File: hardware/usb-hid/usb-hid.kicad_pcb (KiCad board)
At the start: 2 copper layers, 15 parts, among them J1 USB_A, J2 Conn_01x03_Female, J3 Conn_ARM_JTAG_SWD_10, U1 AMS1117-3.3, U2 NRF24L01_Breakout, U3 STM32F103C8Tx, Y1 Crystal

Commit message: Position the components
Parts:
- added C3: C, Capacitor_SMD:C_0603_1608Metric, B.Cu at (141.5, 107.0)
- added C4: C, Capacitor_SMD:C_0603_1608Metric, F.Cu at (132.5, 109.5)
- added C5: C, Capacitor_SMD:C_0603_1608Metric, F.Cu at (129.0, 109.5)
- added C6: C, Capacitor_SMD:C_0603_1608Metric, B.Cu at (138.0, 105.0)
- added J4: Ext_Power, Connector_PinHeader_2.00mm:PinHeader_1x03_P2.00mm_Vertical, F.Cu at (122.0, 104.5)
- added J5: GND, Connector_PinHeader_2.00mm:PinHeader_1x05_P2.00mm_Vertical, F.Cu at (130.5, 77.5)
- added J6: Extra_IO, Connector_PinHeader_2.00mm:PinHeader_1x05_P2.00mm_Vertical, F.Cu at (148.5, 108.5)
- added R4: 10k, Resistor_SMD:R_0603_1608Metric, B.Cu at (138.0, 108.5)
- added R5: 22, Resistor_SMD:R_0603_1608Metric, F.Cu at (128.0, 90.0)
- added R6: 22, Resistor_SMD:R_0603_1608Metric, F.Cu at (128.0, 88.0)
- added R7: 10k, Resistor_SMD:R_0603_1608Metric, F.Cu at (128.0, 84.5)
- added R8: 10k, Resistor_SMD:R_0603_1608Metric, B.Cu at (138.0, 102.5)
- added R9: 100k, Resistor_SMD:R_0603_1608Metric, B.Cu at (141.5, 105.0)
- added SW1: RESET_SW, Button_Switch_SMD:SW_SPST_TL3342, F.Cu at (141.0, 106.0)
- added SW2: EXT_SW, Button_Switch_SMD:SW_SPST_TL3342, F.Cu at (141.5, 98.0)
- C1, C2, R1, R2, U3, Y1: moved to B.Cu
- J1: value USB_A -> PC_USB
- J2: value Conn_01x03_Female -> Debug_UART; footprint Connector_PinHeader_2.00mm:PinHeader_1x03_P2.00mm_Horizontal -> Connector_PinHeader_2.00mm:PinHeader_1x03_P2.00mm_Vertical
- J3: value Conn_ARM_JTAG_SWD_10 -> MCU_SWD
- moved U2 101.5 mm to (148.5, 90.0), turned to 270 degrees
- moved C1 88.3 mm to (143.0, 102.5)
- moved U1 80.7 mm to (130.8, 104.1)
- moved Y1 73.2 mm to (143.0, 90.0), turned to 270 degrees
- moved U3 67.2 mm to (133.8, 89.3), turned to 90 degrees
- moved D1 64.8 mm to (134.5, 97.5), turned to 90 degrees
- moved R2 64.4 mm to (138.0, 97.5)
- moved R1 63.8 mm to (138.0, 100.0)
- moved D3 62.9 mm to (129.5, 97.5), turned to 90 degrees
- moved D2 61.0 mm to (132.0, 97.5), turned to 90 degrees
- moved C2 60.0 mm to (143.0, 77.5)
- moved J2 59.8 mm to (148.0, 77.5)
- moved J1 58.4 mm to (114.3, 88.9), turned to 180 degrees
- moved R3 56.8 mm to (126.2, 98.5), turned to 180 degrees
- moved J3 39.2 mm to (122.0, 77.5), turned to 90 degrees
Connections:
- D1 pad 1: GND -> Net-(D1-Pad1)
- D2 pad 1: GND -> Net-(D2-Pad1)
- D3 pad 1: GND -> Net-(D3-Pad1)
- J1 pad 2: /USB_D- -> Net-(J1-Pad2)
- J1 pad 3: /USB_D+ -> Net-(J1-Pad3)
- R1 pad 1: Net-(D1-Pad2) -> GND
- R1 pad 2: Net-(R1-Pad2) -> Net-(D1-Pad1)
- R2 pad 1: Net-(D2-Pad2) -> GND
- R2 pad 2: Net-(R2-Pad2) -> Net-(D2-Pad1)
- R3 pad 1: Net-(D3-Pad2) -> GND
- R3 pad 2: Net-(R3-Pad2) -> Net-(D3-Pad1)
- U3 pad 10: Net-(R1-Pad2) -> Net-(D1-Pad2)
- U3 pad 11: Net-(R2-Pad2) -> Net-(D2-Pad2)
- U3 pad 12: Net-(R3-Pad2) -> Net-(D3-Pad2)
- U3 pad 18: Net-(U3-Pad18) -> /PWM1
- U3 pad 19: Net-(U3-Pad19) -> /PWM2
- U3 pad 25: Net-(U3-Pad25) -> Net-(U2-Pad4)
- U3 pad 29: Net-(U3-Pad29) -> Net-(U2-Pad8)
- U3 pad 30: Net-(U3-Pad30) -> Net-(U2-Pad3)
- U3 pad 9: Net-(U3-Pad9) -> VCC

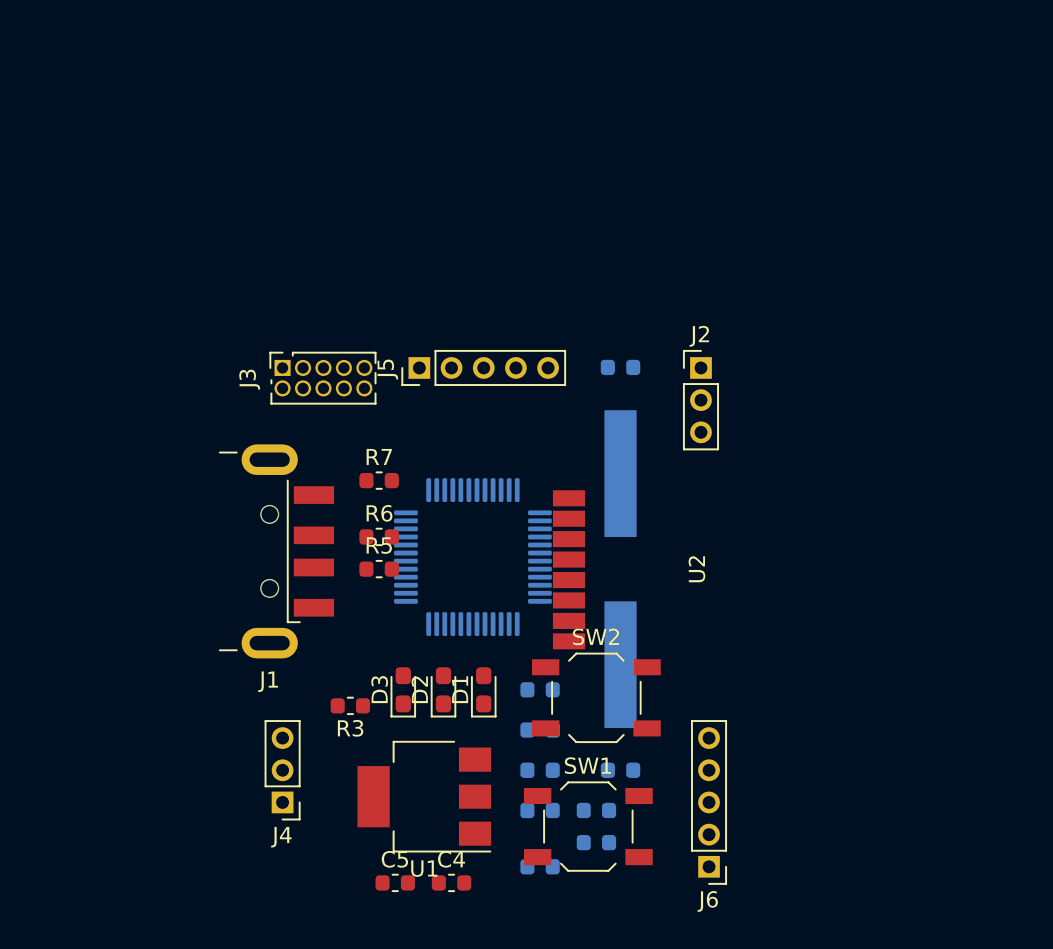
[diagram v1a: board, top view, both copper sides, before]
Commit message: Add new components and make the sizes proper
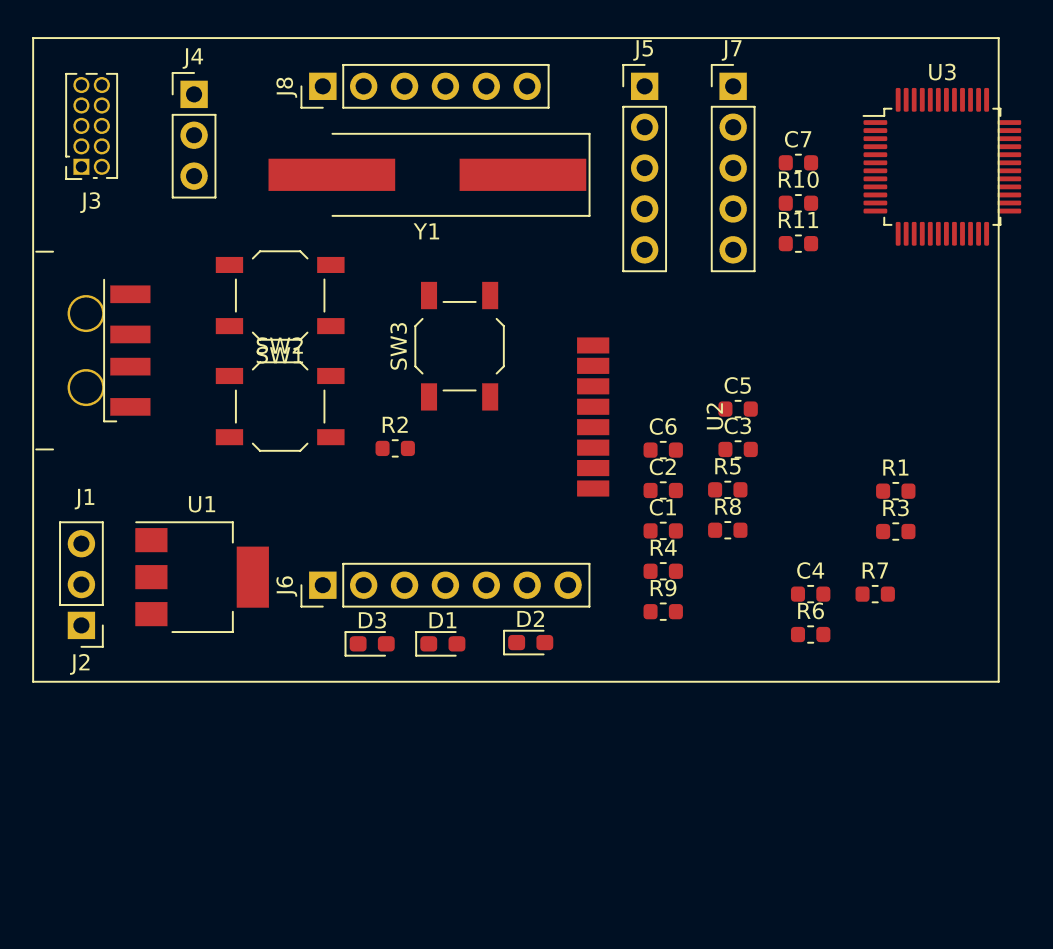
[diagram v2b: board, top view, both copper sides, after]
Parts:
- added C7: C, Capacitor_SMD:C_0603_1608Metric, F.Cu at (154.1, 64.8)
- added J7: Extra-IO-2, Connector_PinHeader_2.54mm:PinHeader_1x05_P2.54mm_Vertical, F.Cu at (150.0, 60.0)
- added J8: Extra-IO-0, Connector_PinHeader_2.54mm:PinHeader_1x06_P2.54mm_Vertical, F.Cu at (124.5, 60.0)
- added R10: 10k, Resistor_SMD:R_0603_1608Metric, F.Cu at (154.1, 67.3)
- added R11: 100k, Resistor_SMD:R_0603_1608Metric, F.Cu at (154.1, 69.8)
- added SW3: EXT_SW, Button_Switch_SMD:SW_SPST_TL3342, F.Cu at (133.0, 76.2)
- C1, C2, C3, C6, R1, R2, R4, R8, R9, U3, Y1: moved to F.Cu
- J1: footprint Connector_USB:USB_A_CNCTech_1001-011-01101_Horizontal -> Connector_USB:USB_A_2.3_2
- J2, J4: footprint Connector_PinHeader_2.00mm:PinHeader_1x03_P2.00mm_Vertical -> Connector_PinHeader_2.54mm:PinHeader_1x03_P2.54mm_Vertical
- J5: footprint Connector_PinHeader_2.00mm:PinHeader_1x05_P2.00mm_Vertical -> Connector_PinHeader_2.54mm:PinHeader_1x05_P2.54mm_Vertical
- J6: value Extra_IO -> Extra-IO-1; footprint Connector_PinHeader_2.00mm:PinHeader_1x05_P2.00mm_Vertical -> Connector_PinHeader_2.54mm:PinHeader_1x07_P2.54mm_Vertical
- moved J4 44.3 mm to (116.5, 60.5), turned to 0 degrees
- moved J2 41.7 mm to (109.5, 93.5), turned to 180 degrees
- moved SW1 38.2 mm to (121.8, 73.0), turned to 180 degrees
- moved U3 37.9 mm to (163.0, 65.0), turned to 0 degrees
- moved C5 36.3 mm to (150.3, 80.1)
- moved R3 35.6 mm to (160.1, 87.7), turned to 0 degrees
- moved R7 31.6 mm to (158.8, 91.6)
- moved J6 29.7 mm to (124.5, 91.0), turned to 90 degrees
- moved C4 28.6 mm to (154.8, 91.6)
- moved R6 27.5 mm to (154.8, 94.1)
- moved Y1 27.3 mm to (131.0, 65.5), turned to 180 degrees
- moved SW2 26.7 mm to (121.8, 79.9)
- moved R1 26.6 mm to (160.1, 85.2)
- moved C3 26.0 mm to (150.3, 82.6)
- moved C6 23.7 mm to (145.7, 82.6)
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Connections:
- J6 pad 1: /PWM1 -> Net-(J6-Pad1)
- J6 pad 2: /PWM2 -> Net-(J6-Pad2)
- U3 pad 15: Net-(J6-Pad3) -> Net-(J7-Pad2)
- U3 pad 16: Net-(J6-Pad4) -> Net-(J7-Pad3)
- U3 pad 17: Net-(J6-Pad5) -> Net-(J7-Pad4)
- U3 pad 18: /PWM1 -> Net-(J6-Pad4)
- U3 pad 19: /PWM2 -> Net-(J6-Pad3)
- U3 pad 2: Net-(U3-Pad2) -> Net-(J6-Pad7)
- U3 pad 20: Net-(U3-Pad20) -> Net-(J6-Pad2)
- U3 pad 3: Net-(U3-Pad3) -> Net-(J6-Pad6)
- U3 pad 39: Net-(U3-Pad39) -> Net-(J6-Pad1)
- U3 pad 4: Net-(U3-Pad4) -> Net-(J6-Pad5)

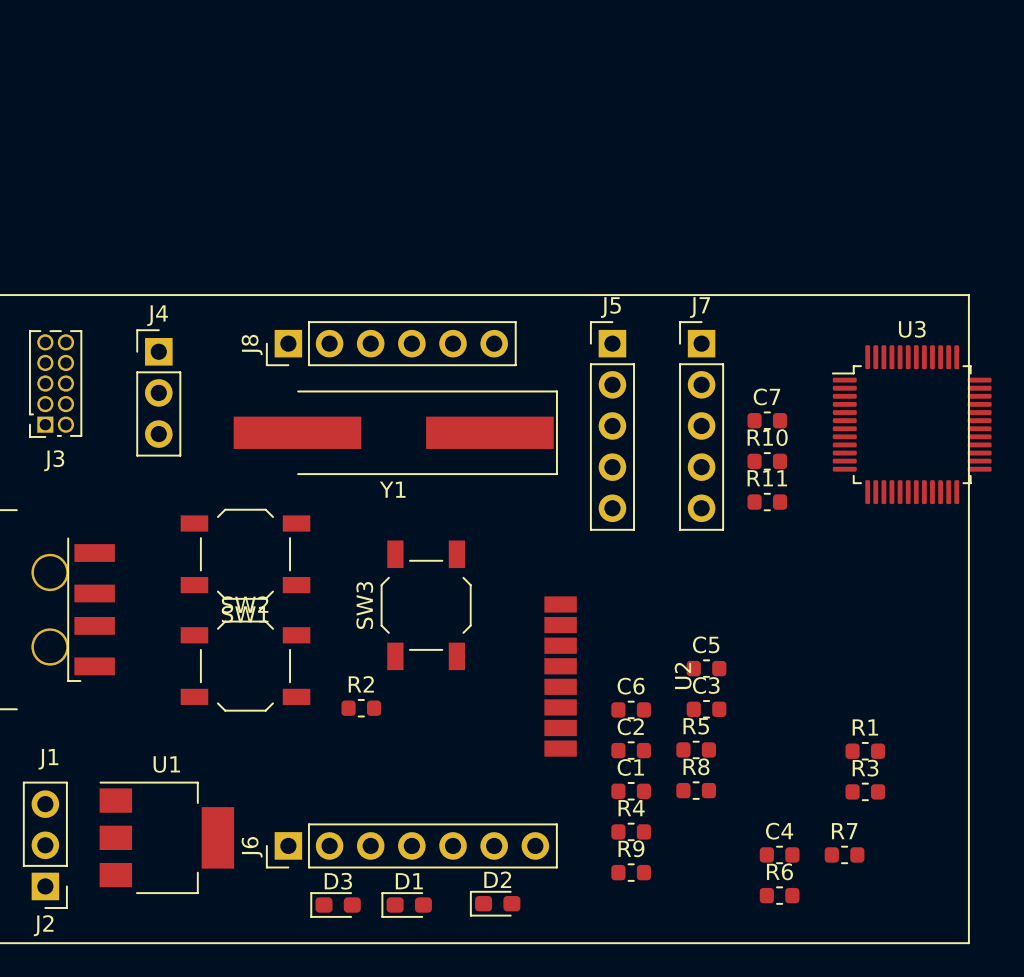
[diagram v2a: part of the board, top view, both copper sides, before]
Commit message: Restruct the schematic for better symbols
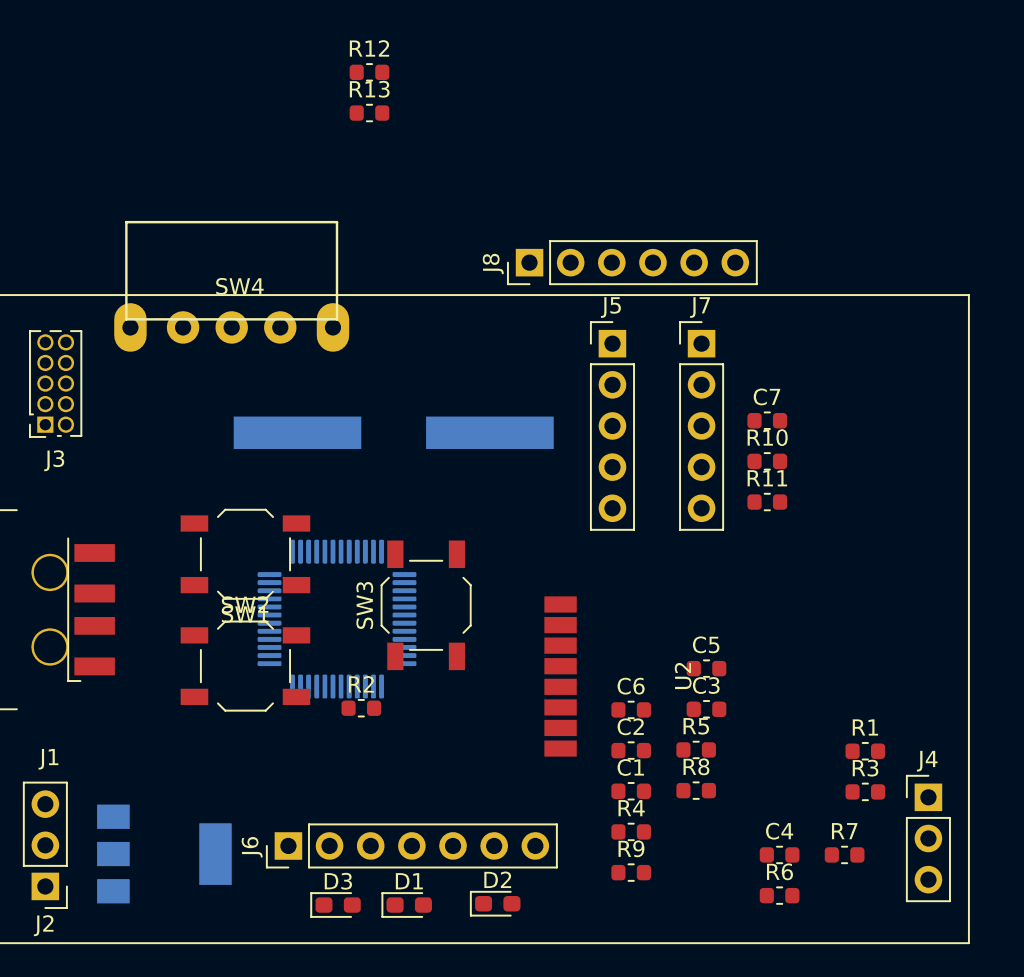
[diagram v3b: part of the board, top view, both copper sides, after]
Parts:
- added R12: 0, Resistor_SMD:R_0603_1608Metric, F.Cu at (129.5, 43.3)
- added R13: 0, Resistor_SMD:R_0603_1608Metric, F.Cu at (129.5, 45.8)
- added SW4: Power_SW, custom_lib:Switch-SS12F23, F.Cu at (121.0, 59.0)
- U1, U3, Y1: moved to B.Cu
- moved J4 54.9 mm to (164.0, 88.0)
- moved U3 37.5 mm to (127.5, 77.0), turned to 180 degrees
- moved J8 15.7 mm to (139.4, 55.0)
- moved U1 1.01 mm to (116.8, 91.5)
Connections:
- J4 pad 1: VCC -> Net-(J4-Pad1)
- J4 pad 3: Net-(J1-Pad1) -> Net-(J4-Pad3)

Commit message: Finish layout
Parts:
- removed R12, R13: 0, Resistor_SMD:R_0603_1608Metric
- added C8: C, Capacitor_SMD:C_0603_1608Metric, F.Cu at (60.1, 79.7)
- C1, C2, C3, C4, C5, R1, R2, R3: moved to B.Cu
- J5: value GND -> Extra-IO-2; footprint Connector_PinHeader_2.54mm:PinHeader_1x05_P2.54mm_Vertical -> Connector_PinHeader_2.54mm:PinHeader_1x06_P2.54mm_Vertical
- J6: footprint Connector_PinHeader_2.54mm:PinHeader_1x07_P2.54mm_Vertical -> Connector_PinHeader_2.54mm:PinHeader_1x06_P2.54mm_Vertical
- J7: value Extra-IO-2 -> Conn_01x02_Female; footprint Connector_PinHeader_2.54mm:PinHeader_1x05_P2.54mm_Vertical -> Connector_PinHeader_2.54mm:PinHeader_1x02_P2.54mm_Vertical
- R10: value 10k -> 22; moved to B.Cu
- R11: value 100k -> 22
- R4, R8: value 10k -> 22
- R7: value 10k -> 1.5k
- SW1: value RESET_SW -> E_SW
- SW2: value EXT_SW -> Reset
- SW3: value EXT_SW -> Boot
- SW4: footprint custom_lib:Switch-SS12F23 -> Button_Switch_THT:SW_Aliexpress_3pin
- U2: value NRF24L01_Breakout -> STM32F103C8; footprint mysensors_radios:NRF24L01-SMD -> mcu:QFP50P900X900X160-48N; moved to B.Cu
- U3: value STM32F103C8Tx -> NRF24L01_SMD; footprint Package_QFP:LQFP-48_7x7mm_P0.5mm -> mysensors_radios:NRF24L01_SMD_PinChange; moved to F.Cu
- moved R7 115.9 mm to (45.9, 65.5), turned to 180 degrees
- moved R1 114.3 mm to (47.3, 66.8)
- moved R6 112.1 mm to (45.9, 67.3), turned to 180 degrees
- moved C4 110.9 mm to (44.1, 85.6)
- moved J7 109.1 mm to (45.5, 91.3), turned to 270 degrees
- moved C7 108.2 mm to (45.9, 63.6), turned to 180 degrees
- moved C2 106.9 mm to (42.3, 57.9)
- moved C5 106.5 mm to (44.1, 87.8)
- moved R5 105.0 mm to (45.9, 69.1), turned to 180 degrees
- moved R9 104.4 mm to (45.9, 61.8), turned to 180 degrees
- moved R3 99.5 mm to (63.6, 63.4), turned to 180 degrees
- moved R11 98.0 mm to (56.1, 66.2)
- moved C6 97.3 mm to (49.7, 66.7)
- moved C3 96.6 mm to (53.9, 75.7)
- moved J4 95.5 mm to (68.6, 91.2), turned to 90 degrees
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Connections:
- C3 pad 1: Net-(C3-Pad1) -> VCC
- C3 pad 2: GND -> /SW_conn
- C6 pad 1: VCC -> /NRST
- C6 pad 2: Net-(C6-Pad2) -> GND
- C7 pad 1: VCC -> /Boot1
- C7 pad 2: Net-(C7-Pad2) -> GND
- D1 pad 1: Net-(D1-Pad1) -> GND
- D2 pad 1: Net-(D2-Pad1) -> GND
- D3 pad 1: Net-(D3-Pad1) -> GND
- J3 pad 10: Net-(J3-Pad10) -> (no net)
- J3 pad 2: Net-(J3-Pad2) -> /SWDIO_Conn
- J3 pad 4: Net-(J3-Pad4) -> /SWDCLK_Conn
- J3 pad 6: Net-(J3-Pad6) -> (no net)
- J3 pad 7: Net-(J3-Pad7) -> (no net)
- J3 pad 8: Net-(J3-Pad8) -> (no net)
- J3 pad 9: Net-(J3-Pad9) -> (no net)
- J5 pad 1: GND -> Net-(J5-Pad1)
- J5 pad 2: GND -> Net-(J5-Pad2)
- J5 pad 3: GND -> Net-(J5-Pad3)
- J5 pad 4: GND -> Net-(J5-Pad4)
- J5 pad 5: GND -> Net-(J5-Pad5)
- J7 pad 1: Net-(J7-Pad1) -> VCC
- J7 pad 2: Net-(J7-Pad2) -> GND
- R1 pad 1: GND -> Net-(D1-Pad2)
- R1 pad 2: Net-(D1-Pad1) -> Net-(R1-Pad2)
- R10 pad 1: Net-(C7-Pad2) -> GND
- R11 pad 1: GND -> /NRST
- R11 pad 2: Net-(R10-Pad2) -> VCC
- R2 pad 1: GND -> Net-(D2-Pad2)
- R2 pad 2: Net-(D2-Pad1) -> Net-(R2-Pad2)
- R3 pad 1: GND -> Net-(D3-Pad2)
- R3 pad 2: Net-(D3-Pad1) -> Net-(R3-Pad2)
- R4 pad 1: Net-(C3-Pad1) -> /SW_conn
- R4 pad 2: VCC -> Net-(R4-Pad2)
- R8 pad 1: Net-(C6-Pad2) -> GND
- R8 pad 2: Net-(R8-Pad2) -> Net-(R4-Pad2)
- R9 pad 1: GND -> /Boot1
- R9 pad 2: Net-(R8-Pad2) -> GND
- SW1 pad 1: GND -> VCC
- SW1 pad 2: Net-(C3-Pad1) -> Net-(R4-Pad2)
- SW2 pad 1: VCC -> /NRST
- SW2 pad 2: Net-(R8-Pad2) -> GND
- SW3 pad 2: Net-(R10-Pad2) -> /Boot1
- SW4 pad 2: Net-(R12-Pad1) -> Net-(J1-Pad1)
- U2 pad 1: GND -> VCC
- U2 pad 2: VCC -> Net-(J8-Pad6)
- U2 pad 3: Net-(U2-Pad3) -> Net-(J8-Pad5)
- U2 pad 4: Net-(U2-Pad4) -> Net-(J8-Pad4)
- U2 pad 5: Net-(U2-Pad5) -> Net-(C2-Pad2)
- U2 pad 6: Net-(U2-Pad6) -> Net-(C1-Pad2)
- U2 pad 7: Net-(U2-Pad7) -> /NRST
- U2 pad 8: Net-(U2-Pad8) -> GND
- U3 pad 1: Net-(U3-Pad1) -> VCC
- U3 pad 2: Net-(J6-Pad7) -> GND
- U3 pad 3: Net-(J6-Pad6) -> Net-(U2-Pad30)
- U3 pad 4: Net-(J6-Pad5) -> Net-(U2-Pad29)
- U3 pad 5: Net-(C2-Pad2) -> Net-(U2-Pad26)
- U3 pad 6: Net-(C1-Pad2) -> Net-(U2-Pad28)
- U3 pad 7: Net-(C3-Pad1) -> Net-(U2-Pad27)
- U3 pad 8: GND -> Net-(U2-Pad25)
- Y1 pad 1: Net-(C1-Pad2) -> Net-(C2-Pad2)
- Y1 pad 2: Net-(C2-Pad2) -> Net-(C1-Pad2)
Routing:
- net GND: track 0.00 -> 265.9 mm, vias 0 -> 4
- net VCC: track 0.00 -> 115.3 mm, vias 0 -> 5
- net Net-(U2-Pad25): track 0.00 -> 56.2 mm, vias 0 -> 1
- net Net-(U2-Pad27): track 0.00 -> 56.1 mm, vias 0 -> 1
- net Net-(J1-Pad1): track 0.00 -> 41.0 mm, vias 0 -> 1
- net /SWDCLK_Conn: track 0.00 -> 37.2 mm, vias 0 -> 1
- net Net-(J6-Pad6): track 0.00 -> 27.8 mm, vias 0 -> 1
- net /SWDIO_Conn: track 0.00 -> 26.4 mm, vias 0 -> 1
- net Net-(J6-Pad5): track 0.00 -> 26.2 mm, vias 0 -> 1
- net Net-(J6-Pad4): track 0.00 -> 23.7 mm, vias 0 -> 1
- net Net-(J6-Pad3): track 0.00 -> 22.4 mm, vias 0 -> 1
- net Net-(J5-Pad6): track 0.00 -> 21.4 mm
- net Net-(J6-Pad2): track 0.00 -> 20.6 mm, vias 0 -> 1
- net Net-(J5-Pad5): track 0.00 -> 19.6 mm
- net Net-(J6-Pad1): track 0.00 -> 19.3 mm, vias 0 -> 1
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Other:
- board outline added: 40.9 x 44.5 mm

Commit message: Move components
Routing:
- added copper zone on B.Cu, net GND
- added copper zone on F.Cu, net GND
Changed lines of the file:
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@@
   (page A4)
   (layers
-    (0 F.Cu signal)
+    (0 F.Cu signal hide)
     (31 B.Cu signal)
     (32 B.Adhes user hide)
-    (33 F.Adhes user hide)
-    (34 B.Paste user)
-    (35 F.Paste user hide)
+    (33 F.Adhes user)
+    (34 B.Paste user hide)
+    (35 F.Paste user)
     (36 B.SilkS user hide)
-    (37 F.SilkS user hide)
-    (38 B.Mask user)
-    (39 F.Mask user hide)
-    (40 Dwgs.User user)
+    (37 F.SilkS user)
+    (38 B.Mask user hide)
+    (39 F.Mask user)
+    (40 Dwgs.User user hide)
     (41 Cmts.User user)
     (42 Eco1.User user)
@@
     (44 Edge.Cuts user)
     (45 Margin user)
-    (46 B.CrtYd user)
+    (46 B.CrtYd user hide)
     (47 F.CrtYd user)
     (48 B.Fab user hide)
@@
   (segment (start 60.8 63.4) (end 62.8 63.4) (width 0.25) (layer B.Cu) (net 50))
   (segment (start 59.78 64.05) (end 60.15 64.05) (width 0.25) (layer B.Cu) (net 50))
+  (zone (net 1) (net_name GND) (layer B.Cu) (hatch edge 0.508)
+    (connect_pads (clearance 0.508))
+    (min_thickness 0.254)
+    (fill yes (arc_segments 32) (thermal_gap 0.508) (thermal_bridge_width 0.508))
+    (polygon
+      (pts
+        (xy 76.65 93.55) (xy 35.85 93.55) (xy 35.8 49.1) (xy 76.7 49.1)
+      )
+    )
+  )
+  (zone (net 1) (net_name GND) (layer F.Cu) (hatch edge 0.508)
+    (connect_pads (clearance 0.508))
+    (min_thickness 0.254)
+    (fill yes (arc_segments 32) (thermal_gap 0.508) (thermal_bridge_width 0.508))
+    (polygon
+      (pts
+        (xy 76.7 49.15) (xy 76.65 93.6) (xy 35.8 93.6) (xy 35.85 49.1)
+      )
+    )
+  )
 )
